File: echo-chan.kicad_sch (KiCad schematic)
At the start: 50 parts, among them J1 SJ1-3533NS, J2 USB_B, SW1 SW_Push, T1 Transformer_1P_1S, U1 JAMMA, U2 JAMMA, U3 AT90USB1286, U4 HD15, U6 THS7374, Y1 16MHz

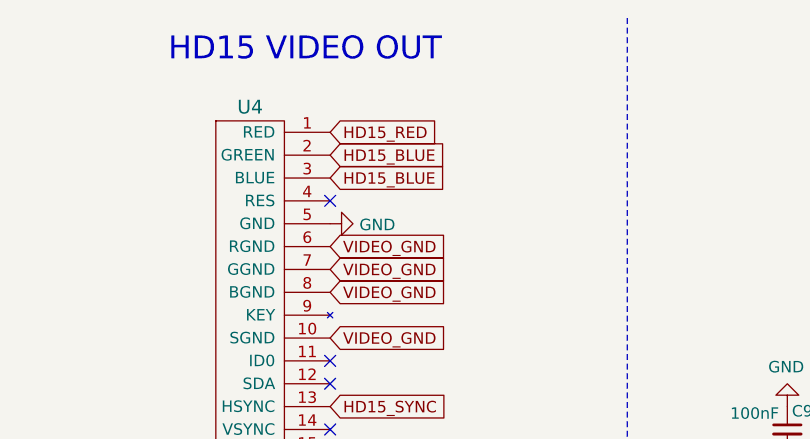
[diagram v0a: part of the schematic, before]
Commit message: [SCHEMATIC] Fix incorrect tag on HD15 green line
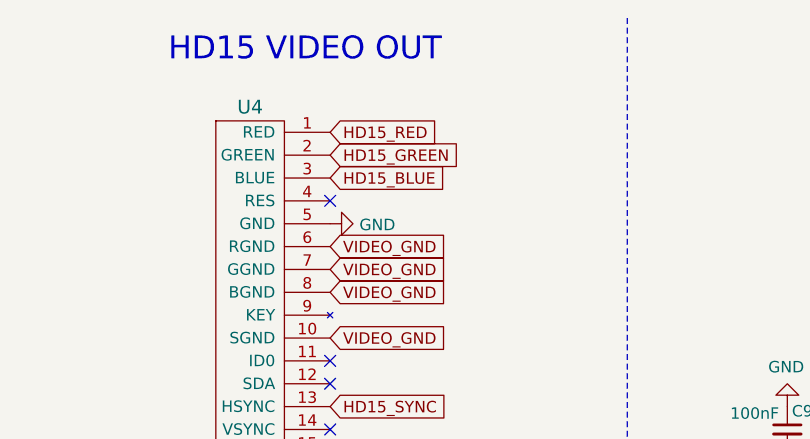
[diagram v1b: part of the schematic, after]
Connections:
- net HD15_BLUE: no longer U4.2 (GREEN)
- net HD15_GREEN: now also U4.2 (GREEN)
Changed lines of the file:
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@@
 		)
 	)
-	(global_label "HD15_BLUE"
+	(global_label "HD15_GREEN"
 		(shape input)
 		(at 135.89 27.94 0)
@@
 		)
 		(property "Intersheetrefs" "${INTERSHEET_REFS}"
-			(at 148.9857 27.94 0)
+			(at 150.3766 27.94 0)
 			(effects
 				(font

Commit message: [PCB] Routing done
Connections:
- net USB_PORT+: now reaches J2.3 (D+), R1.2
- net USB_PORT-: now reaches J2.2 (D-), R2.2
- net USB+ renamed USB_MCU+
- net USB- renamed USB_MCU-
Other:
- moved on the sheet: C7, J2, R1, R2
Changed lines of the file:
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@@
 	)
 	(junction
-		(at 125.73 118.11)
+		(at 115.57 115.57)
 		(diameter 0)
 		(color 0 0 0 0)
@@
 	)
 	(junction
-		(at 137.16 102.87)
+		(at 127 100.33)
 		(diameter 0)
 		(color 0 0 0 0)
@@
 	(wire
 		(pts
-			(xy 137.16 102.87) (xy 140.97 102.87)
+			(xy 127 100.33) (xy 130.81 100.33)
 		)
 		(stroke
@@
 	(wire
 		(pts
-			(xy 133.35 102.87) (xy 137.16 102.87)
+			(xy 123.19 100.33) (xy 127 100.33)
 		)
 		(stroke
@@
 	(wire
 		(pts
-			(xy 123.19 118.11) (xy 125.73 118.11)
+			(xy 113.03 115.57) (xy 115.57 115.57)
 		)
 		(stroke
@@
 	(wire
 		(pts
-			(xy 137.16 100.33) (xy 137.16 102.87)
+			(xy 127 97.79) (xy 127 100.33)
 		)
 		(stroke
@@
 		)
 	)
+	(global_label "USB_PORT+"
+		(shape input)
+		(at 123.19 105.41 0)
+		(fields_autoplaced yes)
+		(effects
+			(font
+				(size 1.27 1.27)
+			)
+			(justify left)
+		)
+		(property "Intersheetrefs" "${INTERSHEET_REFS}"
+			(at 136.7091 105.41 0)
+			(effects
+				(font
+					(size 1.27 1.27)
+				)
+				(justify left)
+				(hide yes)
+			)
+		)
+	)
 	(global_label "P1_B4"
 		(shape input)
@@
 		)
 	)
-	(global_label "USB-"
+	(global_label "USB_MCU-"
 		(shape input)
-		(at 140.97 110.49 0)
+		(at 147.32 116.84 0)
 		(fields_autoplaced yes)
 		(effects
@@
 		)
 		(property "Intersheetrefs" "${INTERSHEET_REFS}"
-			(at 148.6834 110.49 0)
+			(at 160.0529 116.84 0)
 			(effects
 				(font
@@
 		)
 	)
-	(global_label "USB-"
+	(global_label "USB_MCU-"
 		(shape input)
 		(at 201.93 66.04 180)
@@
 		)
 		(property "Intersheetrefs" "${INTERSHEET_REFS}"
-			(at 194.2166 66.04 0)
+			(at 189.1971 66.04 0)
 			(effects
 				(font
@@
 		)
 	)
-	(global_label "USB+"
+	(global_label "USB_MCU+"
 		(shape input)
 		(at 201.93 68.58 180)
@@
 		)
 		(property "Intersheetrefs" "${INTERSHEET_REFS}"
-			(at 194.2166 68.58 0)
+			(at 189.1971 68.58 0)
 			(effects
 				(font
@@
 		)
 	)
+	(global_label "USB_PORT-"
+		(shape input)
+		(at 123.19 107.95 0)
+		(fields_autoplaced yes)
+		(effects
+			(font
+				(size 1.27 1.27)
+			)
+			(justify left)
+		)
+		(property "Intersheetrefs" "${INTERSHEET_REFS}"
+			(at 136.7091 107.95 0)
+			(effects
+				(font
+					(size 1.27 1.27)
+				)
+				(justify left)
+				(hide yes)
+			)
+		)
+	)
 	(global_label "COIN_LOCK_2"
 		(shape input)
@@
 	(global_label "VBUS"
 		(shape input)
-		(at 140.97 102.87 0)
+		(at 130.81 100.33 0)
 		(fields_autoplaced yes)
 		(effects
@@
 		)
 		(property "Intersheetrefs" "${INTERSHEET_REFS}"
-			(at 148.1996 102.87 0)
+			(at 138.0396 100.33 0)
 			(effects
 				(font
@@
 		)
 	)
+	(global_label "USB_PORT+"
+		(shape input)
+		(at 139.7 114.3 180)
+		(fields_autoplaced yes)
+		(effects
+			(font
+				(size 1.27 1.27)
+			)
+			(justify right)
+		)
+		(property "Intersheetrefs" "${INTERSHEET_REFS}"
+			(at 126.1809 114.3 0)
+			(effects
+				(font
+					(size 1.27 1.27)
+				)
+				(justify right)
+				(hide yes)
+			)
+		)
+	)
 	(global_label "P2_RIGHT"
 		(shape input)
@@
 		)
 	)
-	(global_label "USB+"
+	(global_label "USB_MCU+"
 		(shape input)
-		(at 140.97 107.95 0)
+		(at 147.32 114.3 0)
 		(fields_autoplaced yes)
 		(effects
@@
 		)
 		(property "Intersheetrefs" "${INTERSHEET_REFS}"
-			(at 148.6834 107.95 0)
+			(at 160.0529 114.3 0)
 			(effects
 				(font
@@
 		)
 	)
+	(global_label "USB_PORT-"
+		(shape input)
+		(at 139.7 116.84 180)
+		(fields_autoplaced yes)
+		(effects
+			(font
+				(size 1.27 1.27)
+			)
+			(justify right)
+		)
+		(property "Intersheetrefs" "${INTERSHEET_REFS}"
+			(at 126.1809 116.84 0)
+			(effects
+				(font
+					(size 1.27 1.27)
+				)
+				(justify right)
+				(hide yes)
+			)
+		)
+	)
 	(global_label "COIN_LOCK_2"
 		(shape input)
@@
 	(symbol
 		(lib_id "jamma-streamer-rescue:R-jamma-streamer-rescue")
-		(at 137.16 107.95 270)
+		(at 143.51 114.3 270)
 		(unit 1)
 		(exclude_from_sim no)
@@
 		(dnp no)
 		(property "Reference" "R1"
-			(at 137.16 105.41 90)
+			(at 143.51 112.268 90)
 			(effects
 				(font
@@
 		)
 		(property "Value" "22"
-			(at 137.16 107.95 90)
+			(at 143.51 114.3 90)
 			(effects
 				(font
@@
 		)
 		(property "Footprint" "Resistor_SMD:R_0805_2012Metric"
-			(at 137.16 106.172 90)
+			(at 143.51 112.522 90)
 			(effects
 				(font
@@
 		)
 		(property "Datasheet" ""
-			(at 137.16 107.95 0)
+			(at 143.51 114.3 0)
 			(effects
 				(font
@@
 		)
 		(property "Description" ""
-			(at 137.16 107.95 0)
+			(at 143.51 114.3 0)
 			(effects
 				(font
@@
 	(symbol
 		(lib_id "jamma-streamer-rescue:R-jamma-streamer-rescue")
-		(at 137.16 110.49 270)
+		(at 143.51 116.84 270)
 		(unit 1)
 		(exclude_from_sim no)
@@
 		(dnp no)
 		(property "Reference" "R2"
-			(at 137.16 112.522 90)
+			(at 143.51 118.872 90)
 			(effects
 				(font
@@
 		)
 		(property "Value" "22"
-			(at 137.16 110.49 90)
+			(at 143.51 116.84 90)
 			(effects
 				(font
@@
 		)
 		(property "Footprint" "Resistor_SMD:R_0805_2012Metric"
-			(at 137.16 108.712 90)
+			(at 143.51 115.062 90)
 			(effects
 				(font
@@
 		)
 		(property "Datasheet" ""
-			(at 137.16 110.49 0)
+			(at 143.51 116.84 0)
 			(effects
 				(font
@@
 		)
 		(property "Description" ""
-			(at 137.16 110.49 0)
+			(at 143.51 116.84 0)
 			(effects
 				(font
@@
 	(symbol
 		(lib_id "jamma-streamer-rescue:USB_B-Connector")
-		(at 125.73 107.95 0)
+		(at 115.57 105.41 0)
 		(unit 1)
 		(exclude_from_sim no)
@@
 		(dnp no)
 		(property "Reference" "J2"
-			(at 129.54 99.06 0)
+			(at 119.38 96.52 0)
 			(effects
 				(font
@@
 		)
 		(property "Value" "USB_B"
-			(at 123.698 99.06 0)
+			(at 113.538 96.52 0)
 			(effects
 				(font
@@
 		)
 		(property "Footprint" "Connector_USB:USB_B_OST_USB-B1HSxx_Horizontal"
-			(at 129.54 109.22 0)
+			(at 119.38 106.68 0)
 			(effects
 				(font
@@
 		)
 		(property "Datasheet" " ~"
-			(at 129.54 109.22 0)
+			(at 119.38 106.68 0)
 			(effects
 				(font
@@
 		)
 		(property "Description" ""
-			(at 125.73 107.95 0)
+			(at 115.57 105.41 0)
 			(effects
 				(font
@@
 	(symbol
 		(lib_id "jamma-streamer-rescue:GND-jamma-streamer-rescue")
-		(at 125.73 118.11 0)
+		(at 115.57 115.57 0)
 		(unit 1)
 		(exclude_from_sim no)
@@
 		(dnp no)
 		(property "Reference" "#PWR0110"
-			(at 125.73 124.46 0)
+			(at 115.57 121.92 0)
 			(effects
 				(font
@@
 		)
 		(property "Value" "GND"
-			(at 125.73 121.92 0)
+			(at 115.57 119.38 0)
 			(effects
 				(font
@@
 		)
 		(property "Footprint" ""
-			(at 125.73 118.11 0)
+			(at 115.57 115.57 0)
 			(effects
 				(font
@@
 		)
 		(property "Datasheet" ""
-			(at 125.73 118.11 0)
+			(at 115.57 115.57 0)
 			(effects
 				(font
@@
 		)
 		(property "Description" ""
-			(at 125.73 118.11 0)
+			(at 115.57 115.57 0)
 			(effects
 				(font
@@
 	(symbol
 		(lib_id "jamma-streamer-rescue:GND-jamma-streamer-rescue")
-		(at 137.16 95.25 180)
+		(at 127 92.71 180)
 		(unit 1)
 		(exclude_from_sim no)
@@
 		(dnp no)
 		(property "Reference" "#PWR01"
-			(at 137.16 88.9 0)
+			(at 127 86.36 0)
 			(effects
 				(font
@@
 		)
 		(property "Value" "GND"
-			(at 137.033 90.8558 0)
+			(at 126.873 88.3158 0)
 			(effects
 				(font
@@
 		)
 		(property "Footprint" ""
-			(at 137.16 95.25 0)
+			(at 127 92.71 0)
 			(effects
 				(font
@@
 		)
 		(property "Datasheet" ""
-			(at 137.16 95.25 0)
+			(at 127 92.71 0)
 			(effects
 				(font
@@
 		)
 		(property "Description" ""
-			(at 137.16 95.25 0)
+			(at 127 92.71 0)
 			(effects
 				(font
@@
 	(symbol
 		(lib_id "Device:C_Small")
-		(at 137.16 97.79 180)
+		(at 127 95.25 180)
 		(unit 1)
 		(exclude_from_sim no)
@@
 		(dnp no)
 		(property "Reference" "C7"
-			(at 135.128 96.012 0)
+			(at 124.968 93.472 0)
 			(effects
 				(font
@@
 		)
 		(property "Value" "1uF"
-			(at 139.7 96.012 0)
+			(at 129.54 93.472 0)
 			(effects
 				(font
@@
 		)
 		(property "Footprint" "Capacitor_SMD:C_0805_2012Metric"
-			(at 137.16 97.79 0)
+			(at 127 95.25 0)
 			(effects
 				(font
@@
 		)
 		(property "Datasheet" "~"
-			(at 137.16 97.79 0)
+			(at 127 95.25 0)
 			(effects
 				(font
@@
 		)
 		(property "Description" ""
-			(at 137.16 97.79 0)
+			(at 127 95.25 0)
 			(effects
 				(font
